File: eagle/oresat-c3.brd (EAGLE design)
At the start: 99.8 x 94.6 mm, 423 parts, among them J5 ORESAT-DEBUG-CONNECTOR-ALL, J6 J-SAMTEC-TFM-120-X1-XXX-D-RA, Q1 MOSFET-PCH-SOT23-6, Q10 PMOS, Q11 FDMQ86530L, Q12 DMP2240UDM-7, Q13 DMP2240UDM-7, Q14 FDMQ86530L, Q2 NTR4101, Q4 NTR4101, Q5 PM45EN, Q6 DMP2240UDM-7, Q7 BFPXXXF, Q8 DMP2240UDM-7, Q9 BFPXXXF, U1 MAX892LEUA+T21-0036K-L, U10 SI4112, U11 U-ONSEMI-AX5043, U12 LP2985AIM5-1.8_NOPB, U13 U-ONSEMI-AX5043, U14 LP2985AIM5-1.8_NOPB, U15 Qorvo 856930, U16 MAC-24+, U17 BP0805A1308, U18 B8666, U19 BP0805A1308, U2 TCAN330, U20 BGB741L7ESD, U21 BP0805A1308, U22 TLV7041DCKRYC5, U23 LP2985AIM5-2.5_NOPB, U24 MAX941EUA+, U25 SN74LVC1G32QDBVRQ1, U26 TPS62112, U27 TPS259620, U28 LP2985AIM5-3.3_NOPB, U29 SN74LVC1G11IDCKRQ1, U3 TCAN330, U30 U-TQP7M9105, U31 BDCN-20-13+, U32 LT5534, U33 LT5534, U34 Micro Crystal RV-3028-C7, U35 FM24CL64B-DGTR, U36 STM32F439VIT6_PORT_BREAKOUT, U4 TPS259621, U5 TPS62111RSA, U6 LP2985AIM5-2.5_NOPB, U7 TLV1704AMPWPSEP, U8 QPC1022, U9 SFEM016GB1EM1TO-A-HG-111-STD, X1 ECS-160-10-36Q-ES-TR_16MHZ, X2 ABS07-32.768KHZ-T-SMD-2, X3 TAITIEN-TY, X4 TAITIEN-TY

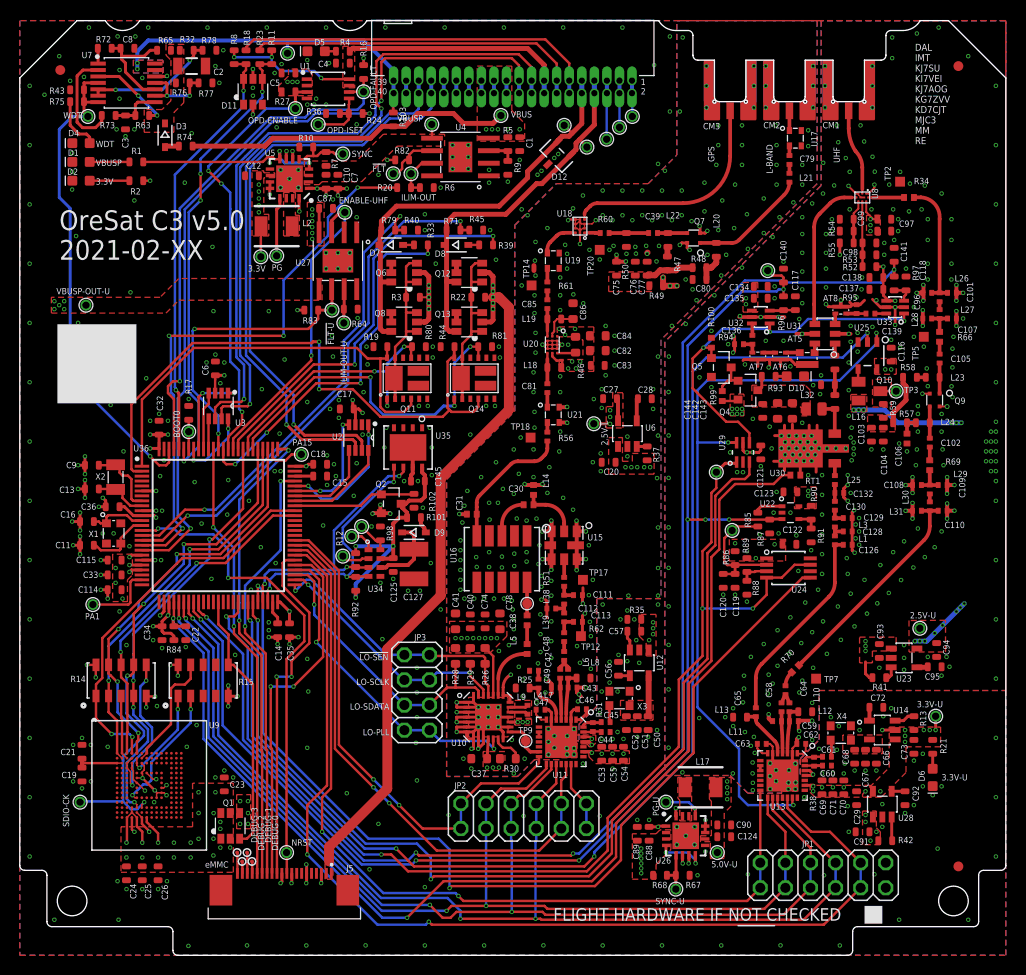
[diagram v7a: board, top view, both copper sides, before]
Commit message: Added pulldowns to M4_PA_ENABLE and TOT_OUT to prevent accidental turn on of the PA. Fixed TOT pin swap of !LATCH and !SHDN. Moved eMMC pull-up resistors to EMMC_VDD so that when the eMMC is powered off, it's not back-powered through the resistors; this still requires the firmware to pull all the eMMC data and clock lines low, however.
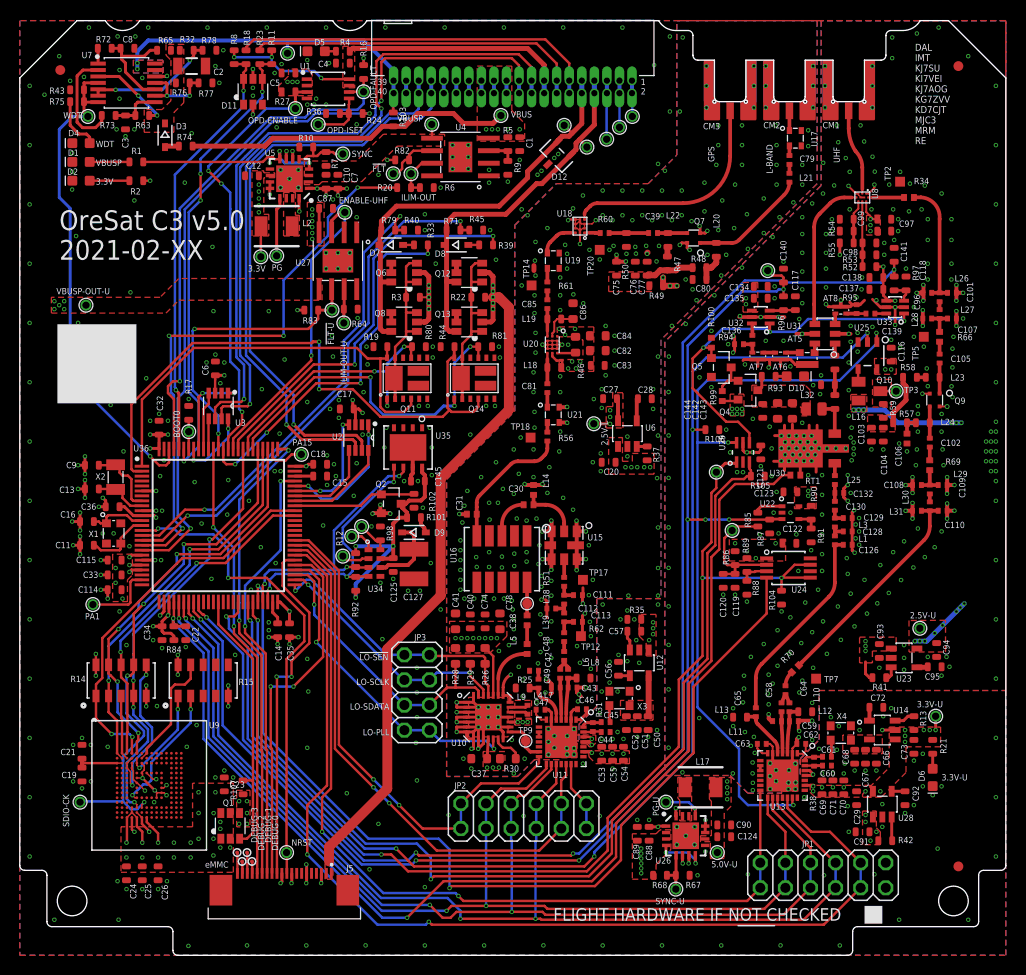
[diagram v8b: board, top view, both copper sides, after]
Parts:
- added R104, R105, R106, R107: 10k, C3_SamacSys_Parts:.0603-C-NOSILK
- moved C122 0.10 mm to (77.9, 41.7)
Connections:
- net !M4_LNA_ENABLE: now also R106.2
- net 3.3V: now also R107.1; no longer R14.10, R14.5, R15.10, R15.5
- net EMMC_PWR: now also R107.2; no longer R15.6
- net EMMC_VDD: now also R14.10, R14.5, R15.10, R15.5
- net GND-U: now also R104.1, R105.1, R106.1
- net M4_PA_ENABLE: now also R105.2
- net M4_TOT_CLEAR: now also U24.4; no longer U24.5
- net TOT_OUT: now also R104.2, U24.5; no longer U24.4
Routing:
- net 3.3V: track 58.7 -> 49.5 mm, vias 76 -> 67
- net EMMC_VDD: track 16.6 -> 25.1 mm, vias 24 -> 32
- net M4_TOT_CLEAR: track 99.9 -> 97.7 mm
- net TOT_OUT: track 117.6 -> 119.6 mm
- net !M4_LNA_ENABLE: track 127.7 -> 129.0 mm, vias 4 -> 5
- net EMMC_PWR: track 26.7 -> 27.4 mm
- net GND-U: vias 338 -> 341
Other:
- board text added: "DAL IMT KJ7SU KI7VEI KJ7AOG KG7ZVV KD7CJT MJC3 MRM RE"
- board text removed: "DAL IMT KJ7SU KI7VEI KJ7AOG KG7ZVV KD7CJT MJC3 MM RE"
